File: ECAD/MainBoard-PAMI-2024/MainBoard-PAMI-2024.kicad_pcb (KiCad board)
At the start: 2 copper layers, 77.4 x 79.3 mm, 3 parts, among them U1 ESP32-S3-WROOM-1

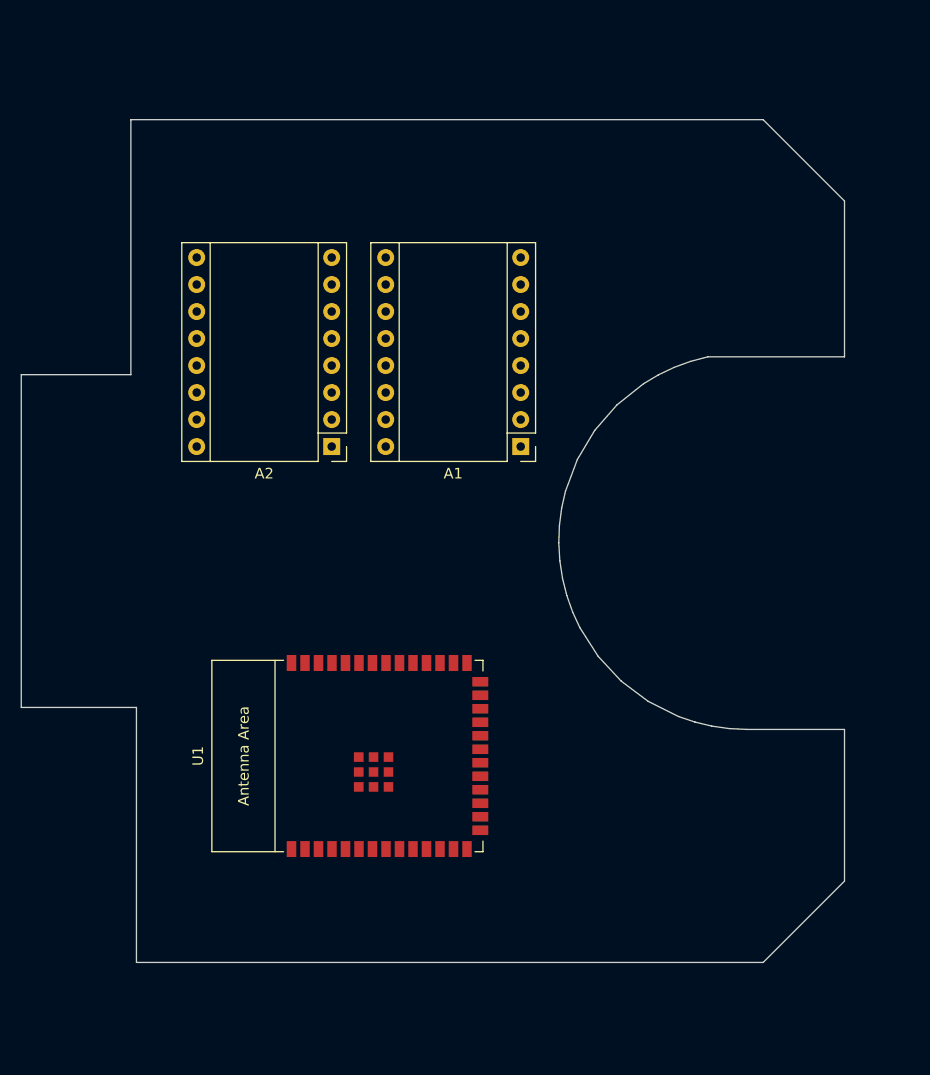
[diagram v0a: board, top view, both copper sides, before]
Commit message: Modify Cut / Add components
Add :
- Connectors
- new Cut
- Regulator
- LEDs
- USB
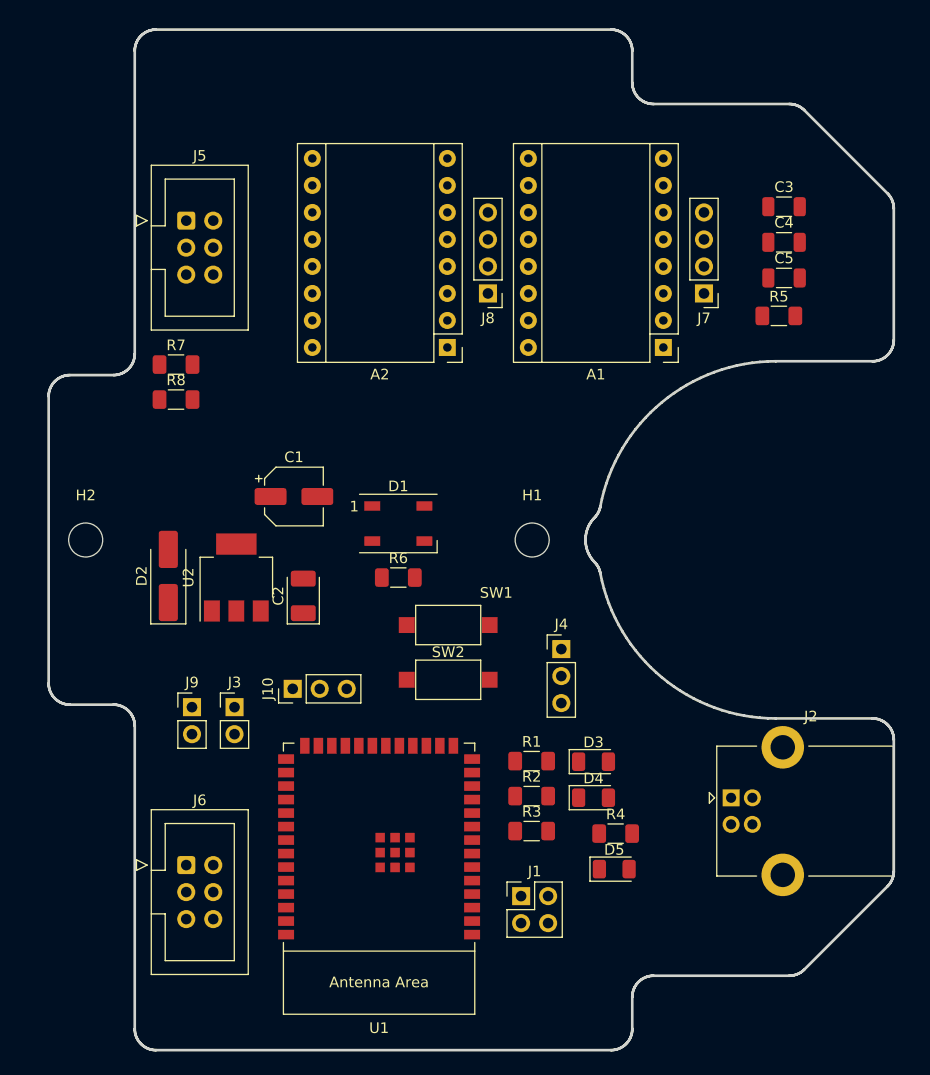
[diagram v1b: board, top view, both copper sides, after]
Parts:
- added C1: 10uF, Capacitor_SMD:CP_Elec_5x5.4, F.Cu at (117.1, 97.4)
- added C2: 22uF, Capacitor_Tantalum_SMD:CP_EIA-3528-12_Kemet-T_Pad1.50x2.35mm_HandSolder, F.Cu at (118.0, 106.8)
- added C3: 1uF/16V, Capacitor_SMD:C_1206_3216Metric, F.Cu at (163.2, 70.2)
- added C4: 0.1uF, Capacitor_SMD:C_1206_3216Metric, F.Cu at (163.2, 73.5)
- added C5: 0.1uF, Capacitor_SMD:C_1206_3216Metric, F.Cu at (163.2, 76.8)
- added D1: WS2812B, LED_SMD:LED_WS2812B_PLCC4_5.0x5.0mm_P3.2mm, F.Cu at (126.9, 100.0)
- added D2: D_Small, Diode_SMD:D_SMA_Handsoldering, F.Cu at (105.3, 104.9)
- added D3: Blue, LED_SMD:LED_1206_3216Metric, F.Cu at (145.3, 122.3)
- added D4: Red, LED_SMD:LED_1206_3216Metric, F.Cu at (145.3, 125.7)
- added D5: Green, LED_SMD:LED_1206_3216Metric, F.Cu at (147.2, 132.5)
- added H1: MountingHole, MountingHole:MountingHole_3.2mm_M3, F.Cu at (139.5, 101.5)
- added H2: MountingHole, MountingHole:MountingHole_3.2mm_M3, F.Cu at (97.5, 101.5)
- added J1: Selecteur-Robot, Connector_PinHeader_2.54mm:PinHeader_2x02_P2.54mm_Vertical, F.Cu at (138.5, 135.0)
- added J10: Serial, Connector_PinHeader_2.54mm:PinHeader_1x03_P2.54mm_Vertical, F.Cu at (117.0, 115.5)
- added J2: USB_B, Connector_USB:USB_B_Lumberg_2411_02_Horizontal, F.Cu at (158.2, 125.8)
- added J3: Tirette, Connector_PinHeader_2.54mm:PinHeader_1x02_P2.54mm_Vertical, F.Cu at (111.5, 117.2)
- added J4: Servo, Connector_PinHeader_2.54mm:PinHeader_1x03_P2.54mm_Vertical, F.Cu at (142.2, 111.8)
- added J5: Sensor_Right, Connector_IDC:IDC-Header_2x03_P2.54mm_Vertical, F.Cu at (107.0, 71.5)
- added J6: Sensor_Left, Connector_IDC:IDC-Header_2x03_P2.54mm_Vertical, F.Cu at (107.0, 132.1)
- added J7: Conn_01x04, Connector_PinHeader_2.54mm:PinHeader_1x04_P2.54mm_Vertical, F.Cu at (155.7, 78.3)
- added J8: Conn_01x04, Connector_PinHeader_2.54mm:PinHeader_1x04_P2.54mm_Vertical, F.Cu at (135.3, 78.3)
- added J9: Tirette, Connector_PinHeader_2.54mm:PinHeader_1x02_P2.54mm_Vertical, F.Cu at (107.5, 117.2)
- added R1: 1K, Resistor_SMD:R_1206_3216Metric_Pad1.30x1.75mm_HandSolder, F.Cu at (139.4, 122.3)
- added R2: 1K, Resistor_SMD:R_1206_3216Metric_Pad1.30x1.75mm_HandSolder, F.Cu at (139.4, 125.6)
- added R3: 330R, Resistor_SMD:R_1206_3216Metric_Pad1.30x1.75mm_HandSolder, F.Cu at (139.4, 128.9)
- added R4: 1K, Resistor_SMD:R_1206_3216Metric_Pad1.30x1.75mm_HandSolder, F.Cu at (147.3, 129.1)
- added R5: 10K, Resistor_SMD:R_1206_3216Metric_Pad1.30x1.75mm_HandSolder, F.Cu at (162.7, 80.4)
- added R6: 330R, Resistor_SMD:R_1206_3216Metric_Pad1.30x1.75mm_HandSolder, F.Cu at (126.9, 105.0)
- added R7: 4K7, Resistor_SMD:R_1206_3216Metric_Pad1.30x1.75mm_HandSolder, F.Cu at (106.0, 85.0)
- added R8: 4K7, Resistor_SMD:R_1206_3216Metric_Pad1.30x1.75mm_HandSolder, F.Cu at (106.0, 88.3)
- added SW1: SW_Push, Button_Switch_SMD:SW_SPST_CK_RS282G05A3, F.Cu at (131.6, 109.5)
- added SW2: SW_Push, Button_Switch_SMD:SW_SPST_CK_RS282G05A3, F.Cu at (131.6, 114.7)
- added U2: AMS1117-3.3, Package_TO_SOT_SMD:SOT-223-3_TabPin2, F.Cu at (111.7, 105.0)
- moved A1 16.3 mm to (151.8, 83.4)
- moved A2 14.3 mm to (131.5, 83.4)
- moved U1 8.54 mm to (125.1, 130.4), turned to 180 degrees
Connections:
- A1 pad 1: unconnected-(A1-GND-Pad1) -> GND
- A1 pad 3: unconnected-(A1-A2-Pad3) -> Net-(A1-A2)
- A1 pad 4: unconnected-(A1-A1-Pad4) -> Net-(A1-A1)
- A1 pad 5: unconnected-(A1-B1-Pad5) -> Net-(A1-B1)
- A1 pad 6: unconnected-(A1-B2-Pad6) -> Net-(A1-B2)
- A1 pad 7: unconnected-(A1-GND-Pad7) -> GND
- A1 pad 8: unconnected-(A1-VMOT-Pad8) -> +5VP
- A2 pad 1: unconnected-(A2-GND-Pad1) -> GND
- A2 pad 3: unconnected-(A2-A2-Pad3) -> Net-(A2-A2)
- A2 pad 4: unconnected-(A2-A1-Pad4) -> Net-(A2-A1)
- A2 pad 5: unconnected-(A2-B1-Pad5) -> Net-(A2-B1)
- A2 pad 6: unconnected-(A2-B2-Pad6) -> Net-(A2-B2)
- A2 pad 7: unconnected-(A2-GND-Pad7) -> GND
- A2 pad 8: unconnected-(A2-VMOT-Pad8) -> +5VP
- U1 pad 1: Net-(U1-GND-Pad1) -> GND
- U1 pad 13: unconnected-(U1-GPIO19/U1RTS/ADC2_CH8/CLK_OUT2/USB_D--Pad13) -> Net-(J2-D-)
- U1 pad 14: unconnected-(U1-GPIO20/U1CTS/ADC2_CH9/CLK_OUT1/USB_D+-Pad14) -> Net-(J2-D+)
- U1 pad 2: unconnected-(U1-3V3-Pad2) -> +3.3V
- U1 pad 27: unconnected-(U1-GPIO0/BOOT-Pad27) -> Boot_Mode
- U1 pad 3: unconnected-(U1-EN-Pad3) -> Chip_PU
- U1 pad 36: unconnected-(U1-U0RXD/GPIO44/CLK_OUT2-Pad36) -> Net-(J10-Pin_1)
- U1 pad 37: unconnected-(U1-U0TXD/GPIO43/CLK_OUT1-Pad37) -> Net-(J10-Pin_2)
- U1 pad 38: unconnected-(U1-GPIO2/TOUCH2/ADC1_CH1-Pad38) -> SCL
- U1 pad 39: unconnected-(U1-GPIO1/TOUCH1/ADC1_CH0-Pad39) -> SDA
- U1 pad 40: Net-(U1-GND-Pad1) -> GND
- U1 pad 41: Net-(U1-GND-Pad1) -> GND
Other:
- board size 77.4 x 79.3 mm -> 79.5 x 96 mm

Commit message: add pen hole and opto sensor
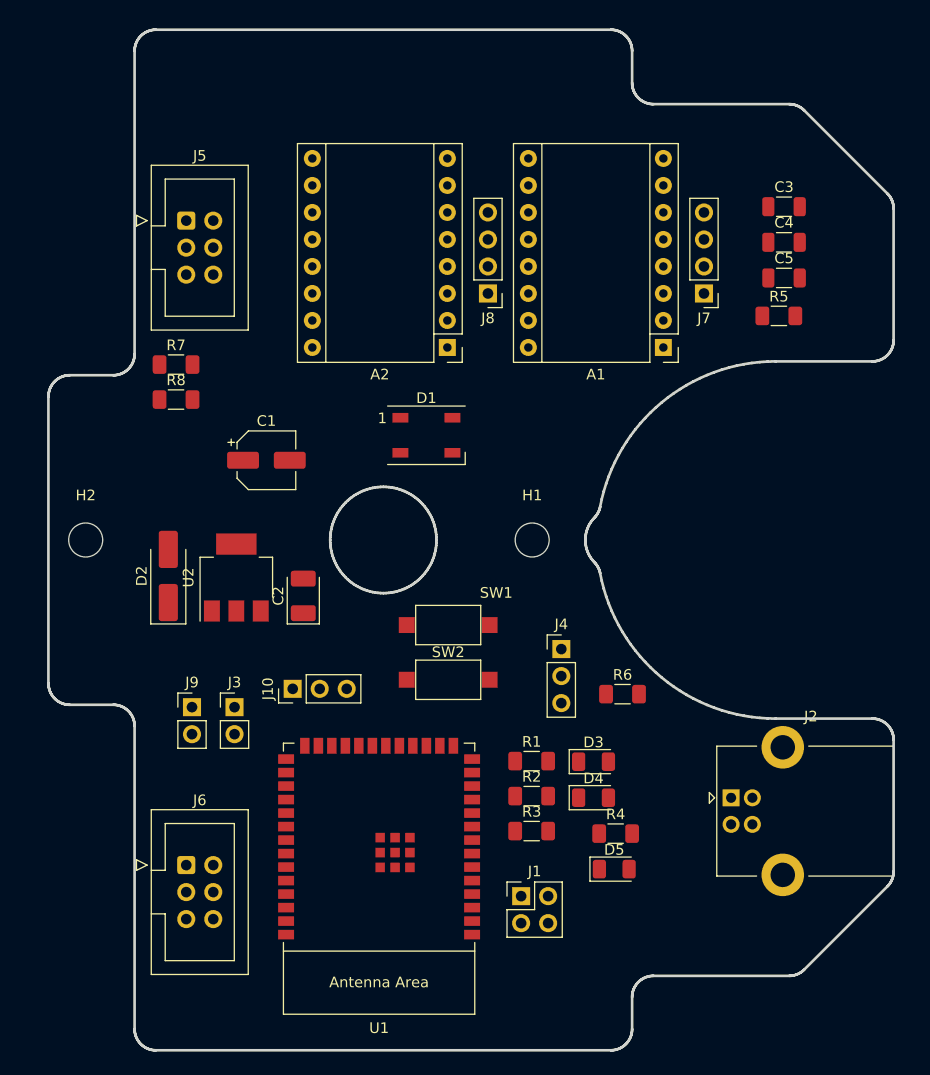
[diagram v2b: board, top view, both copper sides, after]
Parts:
- moved R6 23.8 mm to (148.0, 116.0)
- moved D1 8.71 mm to (129.6, 91.7)
- moved C1 4.28 mm to (114.5, 94.0)
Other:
- outline, holes or cut-outs redrawn

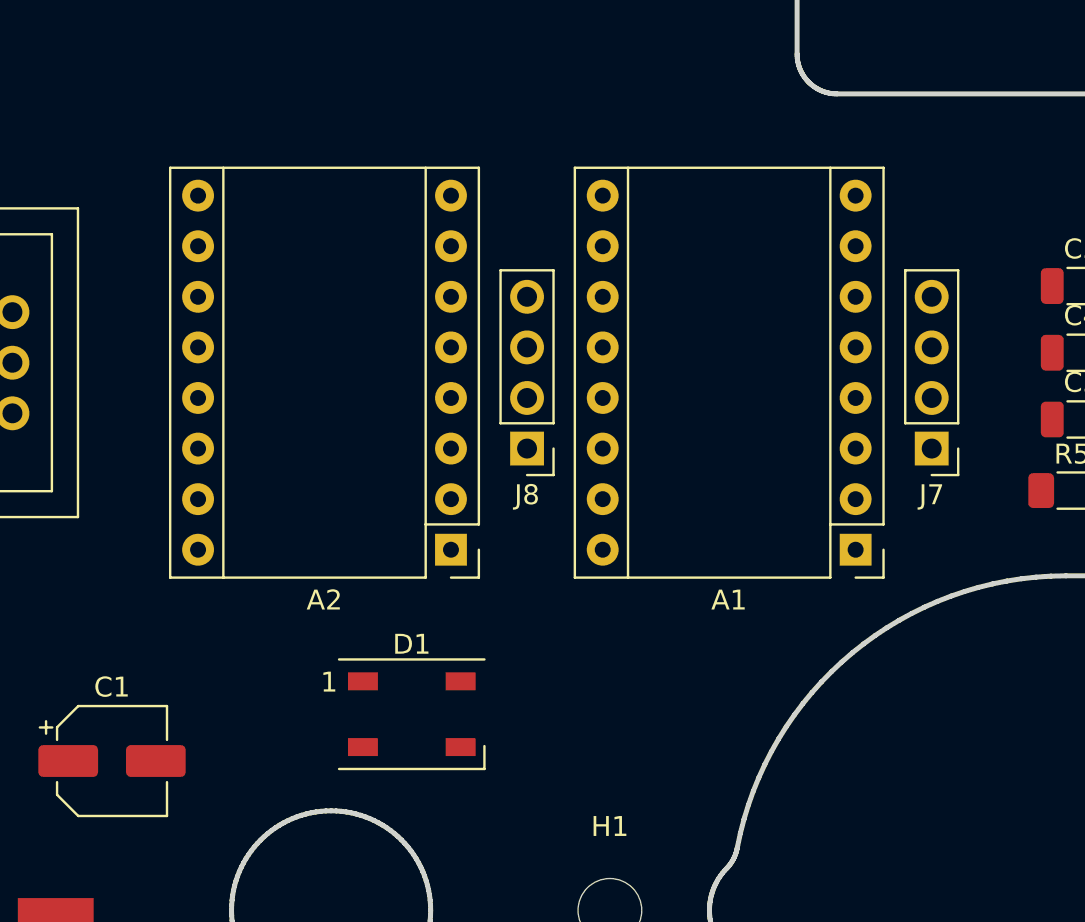
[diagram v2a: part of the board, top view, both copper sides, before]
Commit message: add TMC2208 reorgnise components
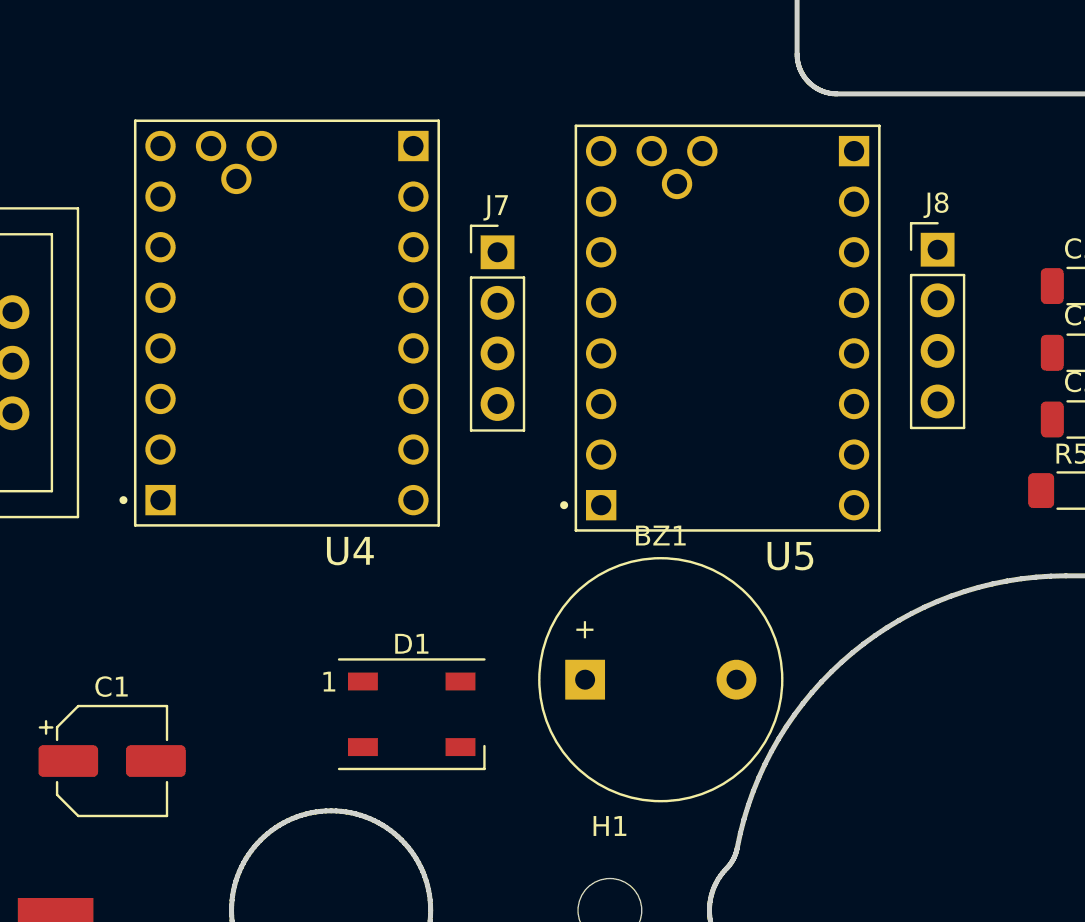
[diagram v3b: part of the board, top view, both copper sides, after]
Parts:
- removed A1, A2: Pololu_Breakout_DRV8825, Module:Pololu_Breakout-16_15.2x20.3mm
- added BZ1: Buzzer, Buzzer_Beeper:Buzzer_12x9.5RM7.6, F.Cu at (138.3, 89.9)
- added U4: TMC2208_SILENTSTEPSTICK, TMC2208_SILENTSTEPSTICK:MODULE_TMC2208_SILENTSTEPSTICK, F.Cu at (123.3, 72.0)
- added U5: TMC2208_SILENTSTEPSTICK, TMC2208_SILENTSTEPSTICK:MODULE_TMC2208_SILENTSTEPSTICK, F.Cu at (145.4, 72.3)
- J7: value Conn_01x04 -> LeftMotor
- J8: value Conn_01x04 -> RightMotor
- J9: value Tirette -> color_team
- SW1: value SW_Push -> SW_EN
- SW2: value SW_Push -> SW_Boot
- moved J7 23.9 mm to (133.9, 68.5), turned to 0 degrees
- moved J8 22.9 mm to (156.0, 68.3), turned to 0 degrees
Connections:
- R7 pad 2: SDA -> SCL
- R8 pad 2: SCL -> SDA
